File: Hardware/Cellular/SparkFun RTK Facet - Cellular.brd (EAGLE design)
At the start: 60 x 34 mm, 79 parts, among them IC1 SN74AVC4T774PW, J2 U.FL, J3 DIAG, Q1 20V/0.2A/8MHz/1.2Ω/1Vth, Q2 310mA/60V/1.6Ω, Q3 310mA/60V/1.6Ω, U1 SARA-R510M8S, U2 74HC1G04, U3 AP2112K-3.3

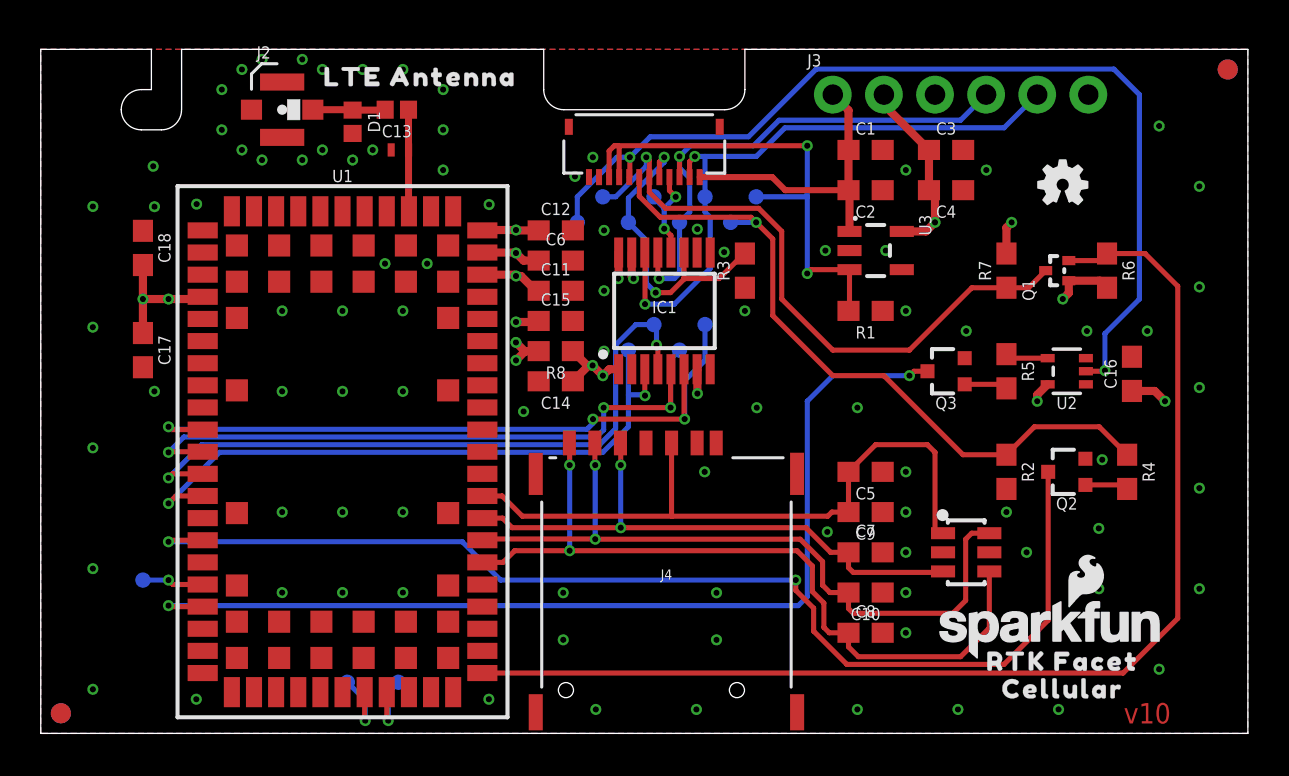
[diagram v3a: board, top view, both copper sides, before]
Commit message: Reduce Main, Connector, Display, and Cell board widths by 1mm to allow for v-score protrusion.
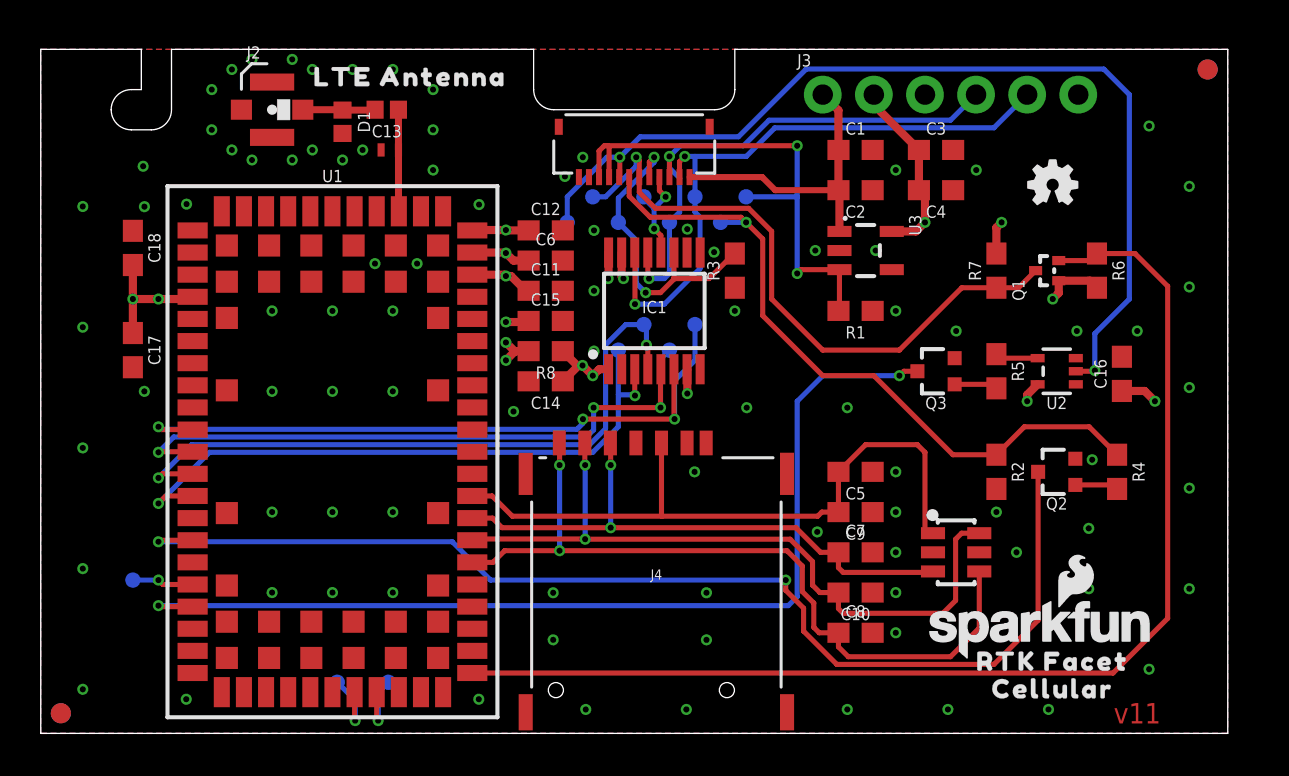
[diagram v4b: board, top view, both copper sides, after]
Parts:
- moved FID2 1.00 mm to (58.0, 33.0)
- moved FID3 1.00 mm to (58.0, 33.0)
- moved C1 0.50 mm to (40.5, 29.0)
- moved C10 0.50 mm to (40.5, 7.00)
- moved C11 0.50 mm to (25.1, 22.0)
- moved C12 0.50 mm to (25.1, 25.0)
- moved C13 0.50 mm to (17.2, 31.0)
- moved C14 0.50 mm to (25.1, 17.5)
- moved C15 0.50 mm to (25.1, 20.5)
- moved C16 0.50 mm to (53.7, 17.9)
- moved C17 0.50 mm to (4.58, 19.1)
- moved C18 0.50 mm to (4.58, 24.1)
- moved C2 0.50 mm to (40.5, 27.0)
- moved C3 0.50 mm to (44.5, 29.0)
- moved C4 0.50 mm to (44.5, 27.0)
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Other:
- board size 60 x 34 mm -> 59 x 34 mm
- board text added: "v11"
- board text removed: "v10"
